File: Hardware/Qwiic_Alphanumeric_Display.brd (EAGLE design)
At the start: 40.6 x 27.9 mm, 44 parts, among them J4 Vertical Qwiic Connector, J5 Vertical Qwiic Connector

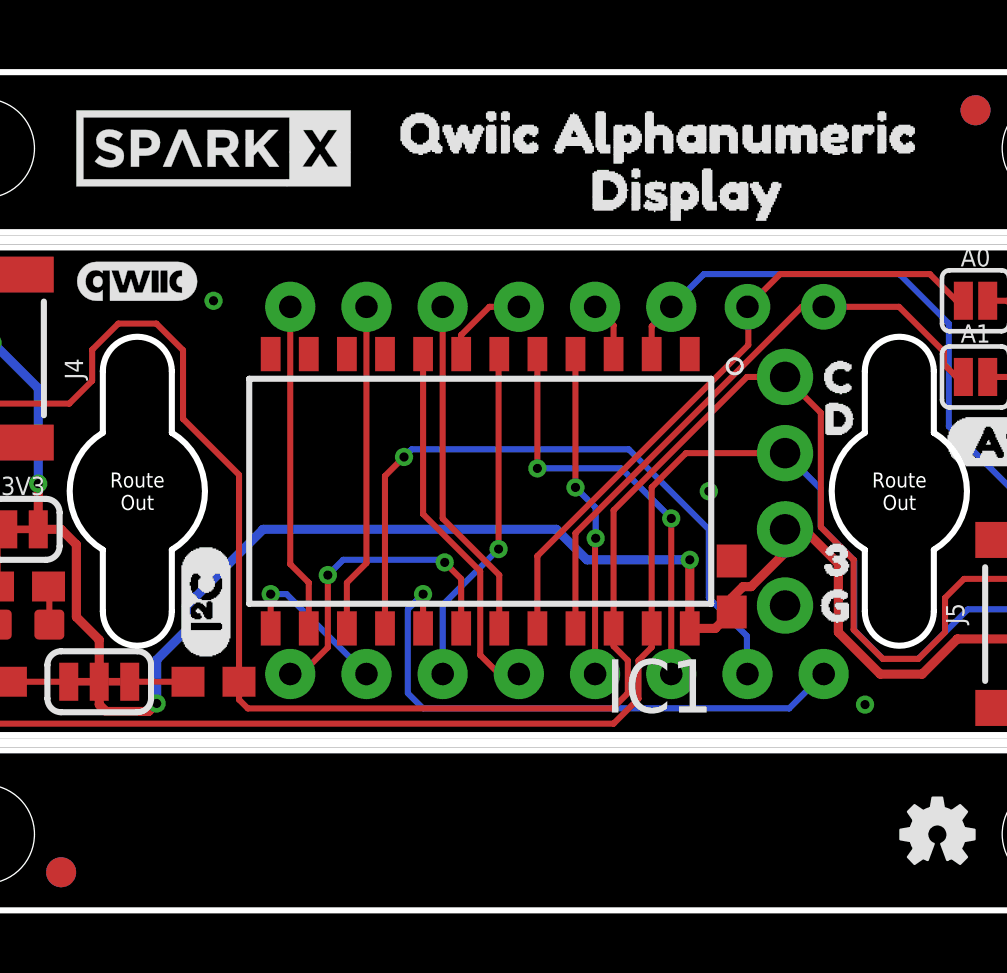
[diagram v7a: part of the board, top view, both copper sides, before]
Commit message: Corrected sch/brd files and production outputs
I seemed to not have the right version of this board when I was wordking from home. Luckily, I had uploaded the files with the double decoupling caps to Sparkle. So I pulled those and fixed this repo...
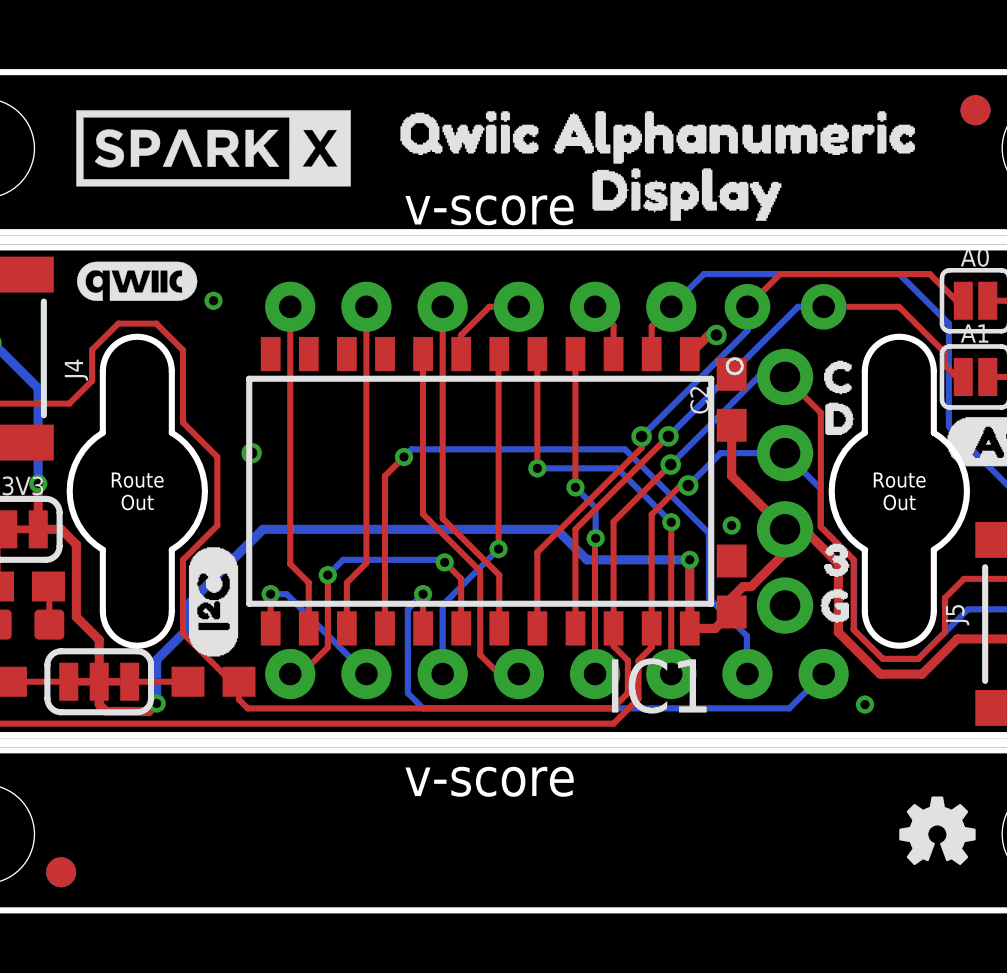
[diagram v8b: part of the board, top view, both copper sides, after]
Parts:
- added C2: 10uF, SparkFun-Capacitors:0603
- C1: value 1.0uF -> 0.1uF
- moved U$10 0.25 mm to (10.2, 9.65)
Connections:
- net 3.3V: now also C2.1
- net GND: now also C2.2
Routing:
- net 3.3V: track 60.6 -> 64.8 mm
- net GND: track 0.00 -> 1.15 mm, vias 4 -> 6
- net SCL: track 68.4 -> 69.3 mm, vias 0 -> 1
- net SDA: track 63.4 -> 62.9 mm, vias 1 -> 2
- net DIG_1A: track 20.4 -> 20.5 mm, vias 0 -> 1
- net DIG_2A: track 21.7 -> 21.6 mm, vias 0 -> 1
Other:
- board text added: "v-score"
